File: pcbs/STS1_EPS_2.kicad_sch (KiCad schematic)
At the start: 12 parts, among them J1 Inter-EPS, J2 DS1, J3 DS2, J4 DS3, J5 DS4, J6 RBF, J7 Antenna Deployment, J8 UCI

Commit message: Worked on STS1_EPS_1 and STS1_EPS_2.
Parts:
- removed J1: Inter-EPS, Connector_PinHeader_2.00mm:PinHeader_2x07_P2.00mm_Vertical, symbol Connector_Generic:Conn_02x07_Odd_Even
- removed TP4: TestPoint, TestPoint:TestPoint_THTPad_D1.0mm_Drill0.5mm, symbol Connector:TestPoint
- added J1: Inter-EPS, Connector_PinHeader_2.00mm:PinHeader_2x10_P2.00mm_Vertical, symbol Connector_Generic:Conn_02x10_Odd_Even
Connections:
- net +5V: now also J1.2 (Pin_2)
- net BATT_RAW: now also J1.18 (Pin_18)
- net DS1_SIGNAL_1: now also J1.11 (Pin_11)
- net DS2_SIGNAL_1: now also J1.12 (Pin_12)
- net GND: now also J1.10 (Pin_10), J1.4 (Pin_4), J1.6 (Pin_6), J1.9 (Pin_9)
- net VOUT_I: now also J1.8 (Pin_8)
- net INTERNAL_V renamed Capacitor Bank/INTERNAL_V
- net Capacitor Bank/INTERNAL_V: now also J1.1 (Pin_1), J1.3 (Pin_3), J1.5 (Pin_5), J1.7 (Pin_7)
- new net BATT: J1.13 (Pin_13), J1.14 (Pin_14), J1.15 (Pin_15), J1.16 (Pin_16)
- new net BATT_I: J1.20 (Pin_20)
- new net CENTER: J1.17 (Pin_17)
- new net NTC: J1.19 (Pin_19)
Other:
- sheet Battery ports: added 5V, BATT, BATT_I, BATT_RAW, BAT_FAULT, CENTER, DS4_SIGNAL_1, NTC; removed none

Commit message: Worked on STS1_EPS_2.
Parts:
- renumbered J2 to J1, J3 to J2, J4 to J3, J5 to J4, J6 to J5, J7 to J6, J1 to J7
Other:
- sheet Battery State Detection ports: added UVLO_SIGNAL; removed none
- sheet Bus Gate ports: added UVLO_SIGNAL; removed none
- moved on the sheet: J8

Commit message: Worked on STS1_EPS_2.
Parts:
- removed J3: DS3, STS_Connector:M808420245, symbol Connector_Generic:Conn_01x02
- removed J4: DS4, STS_Connector:M808420245, symbol Connector_Generic:Conn_01x02
- added R3: 820, Resistor_SMD:R_0805_2012Metric, symbol Device:R
- added U8: TPS259472ARPW, STS_Package_DFN_QFN:TPS259472ARPWR, symbol STS_Power_Management:TPS259472ARPW
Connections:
- net BATT_RAW: now also U8.6 (OUT); no longer J8.1 (Pin_1)
- net GND: now also R3.1, U8.3 (PG), U8.4 (PGTH), U8.8 (GND)
- new net: J8.1 (Pin_1), U8.1 (EN/UVLO), U8.5 (IN)
- new net: R3.2, U8.9 (ILM)
- no-connect marks 4 -> 7
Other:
- sheet Battery ports: added DS1_SIGNAL, DS2_SIGNAL, RBF_SIGNAL, UVLO_SIGNAL; removed 5V, DS4_SIGNAL_1
- sheet Bus Gate ports: added DS1_SIGNAL; removed DS3_SIGNAL
- sheet CSBI ports: added UCI_COBC_UART_[1..2]; removed UCI_COBC_UART[1..2]
- sheet Deployment Switches + RBF ports: added DS1_SIGNAL_3, RBF_SIGNAL_3; removed +5V, DS3+, DS3-, DS3_SIGNAL_1, DS3_SIGNAL_2, DS4+, DS4-, DS4_SIGNAL_1, DS4_SIGNAL_2
- sheet Deployment Timer ports: added none; removed +5V, DS3_SIGNAL, DS4_SIGNAL
- note added: "Ideal diode, that ensures that the battery can not be discharged via the UCI."
- note added: "Sets ~4 A current limit."
- moved on the sheet: J1, J2, J5, J8, TP2

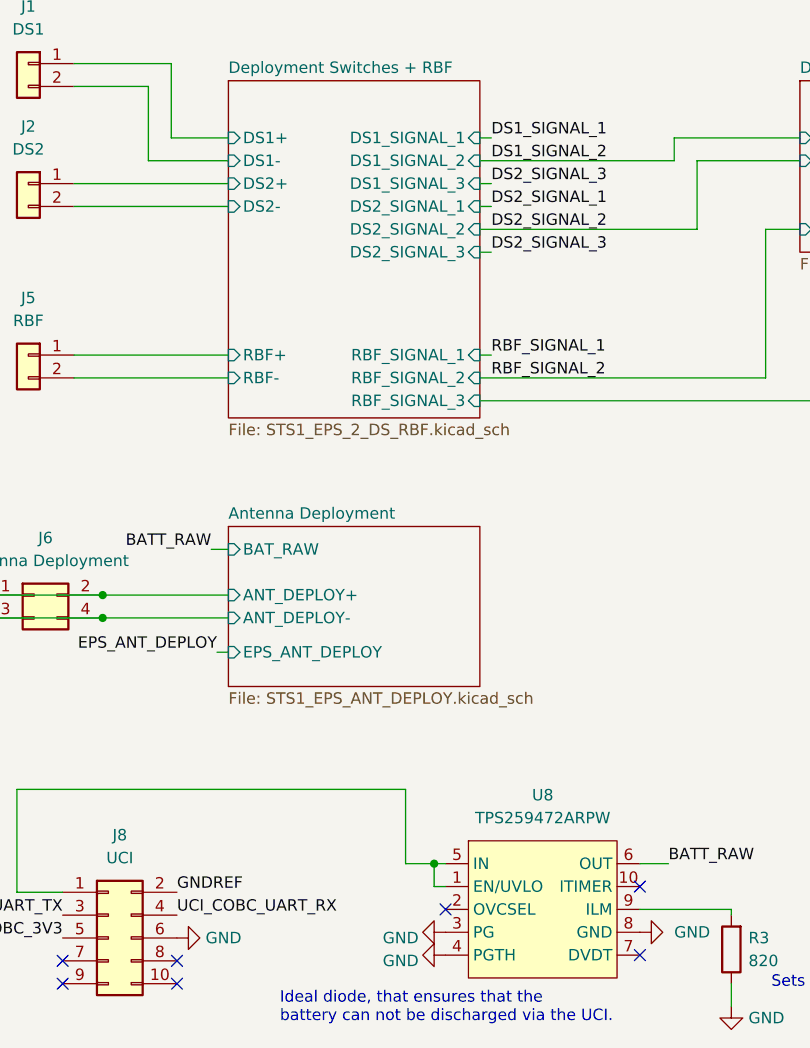
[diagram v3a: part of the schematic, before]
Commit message: STS1_EPS_2 no errors.
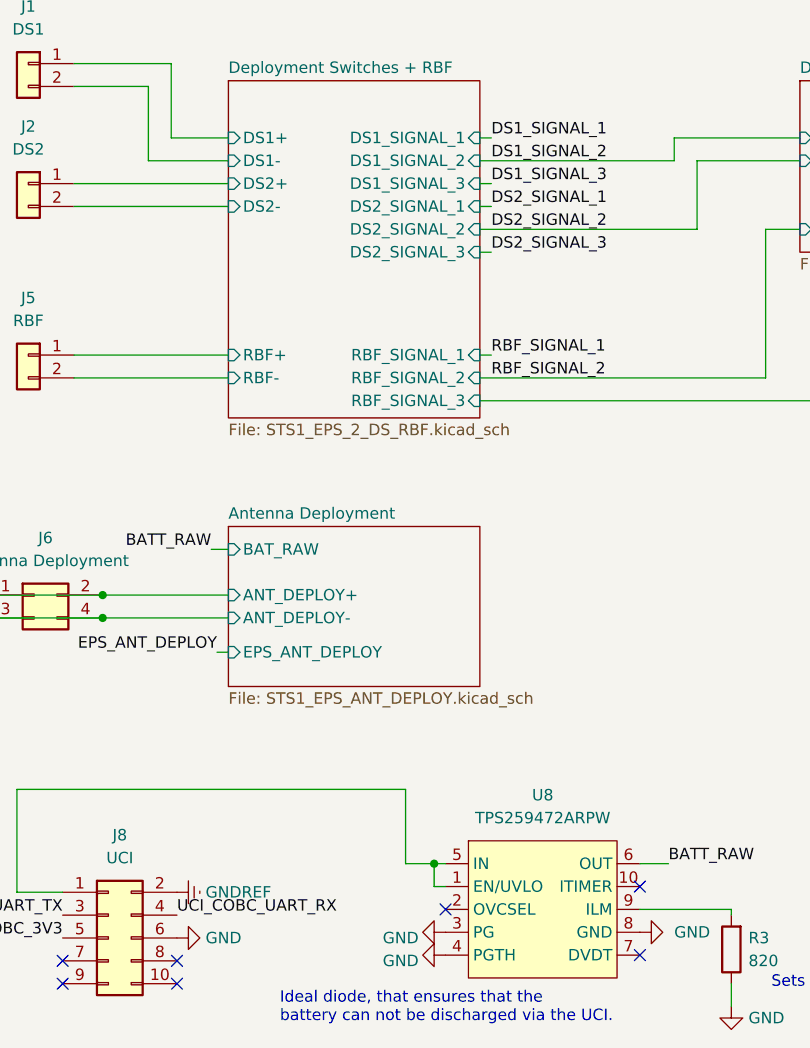
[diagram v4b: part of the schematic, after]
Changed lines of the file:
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@@
     (effects (font (size 1.27 1.27)) (justify left bottom))
   )
-  (label "DS2_SIGNAL_3" (at 78.74 101.6 0)
+  (label "DS1_SIGNAL_3" (at 78.74 101.6 0)
     (effects (font (size 1.27 1.27)) (justify left bottom))
   )
@@
   (label "DS1_SIGNAL_3" (at 190.5 149.225 180)
     (effects (font (size 1.27 1.27)) (justify right bottom))
-  )
-  (label "GNDREF" (at 43.815 180.34 0)
-    (effects (font (size 1.27 1.27)) (justify left bottom))
   )
   (label "BATT_RAW" (at 193.04 109.855 180)
@@
     )
     (property "Datasheet" "" (id 3) (at 40.64 48.26 0)
+      (effects (font (size 1.27 1.27)) hide)
+    )
+    (pin "1")
+  )
+  (symbol (lib_id "power:GNDREF") (at 43.815 180.34 90) (unit 1)
+    (in_bom yes) (on_board yes) (fields_autoplaced)
+    (property "Reference" "#PWR?" (id 0) (at 50.165 180.34 0)
+      (effects (font (size 1.27 1.27)) hide)
+    )
+    (property "Value" "GNDREF" (id 1) (at 46.99 180.3399 90)
+      (effects (font (size 1.27 1.27)) (justify right))
+    )
+    (property "Footprint" "" (id 2) (at 43.815 180.34 0)
+      (effects (font (size 1.27 1.27)) hide)
+    )
+    (property "Datasheet" "" (id 3) (at 43.815 180.34 0)
       (effects (font (size 1.27 1.27)) hide)
     )
@@
       (reference "#PWR0123") (unit 1) (value "~") (footprint "")
     )
+    (path "/782ccd28-d43b-446c-892c-2705ffe9f1f3/2f88d1c3-a8ed-418c-9a0c-3bcf014bd61e"
+      (reference "#PWR0124") (unit 1) (value "GND") (footprint "")
+    )
+    (path "/27387f3b-2bfa-4b28-8ff1-4907e84527b6"
+      (reference "#PWR?") (unit 1) (value "GNDREF") (footprint "")
+    )
     (path "/d08cc104-26df-403e-aeed-bb3c2e21e328/f818a80f-c894-4935-b466-2fb75a773837"
       (reference "C1") (unit 1) (value "100n") (footprint "Capacitor_SMD:C_0805_2012Metric")
@@
       (reference "C4") (unit 1) (value "100n") (footprint "Capacitor_SMD:C_0805_2012Metric")
     )
+    (path "/782ccd28-d43b-446c-892c-2705ffe9f1f3/bab6904b-9018-41a1-928c-c75a76fad2c6"
+      (reference "C5") (unit 1) (value "100n") (footprint "Capacitor_SMD:C_0805_2012Metric")
+    )
     (path "/f1424bad-2b95-4d34-bc23-e338e9fb6fbb/723f186f-e509-4f79-b697-dbc3026f5475"

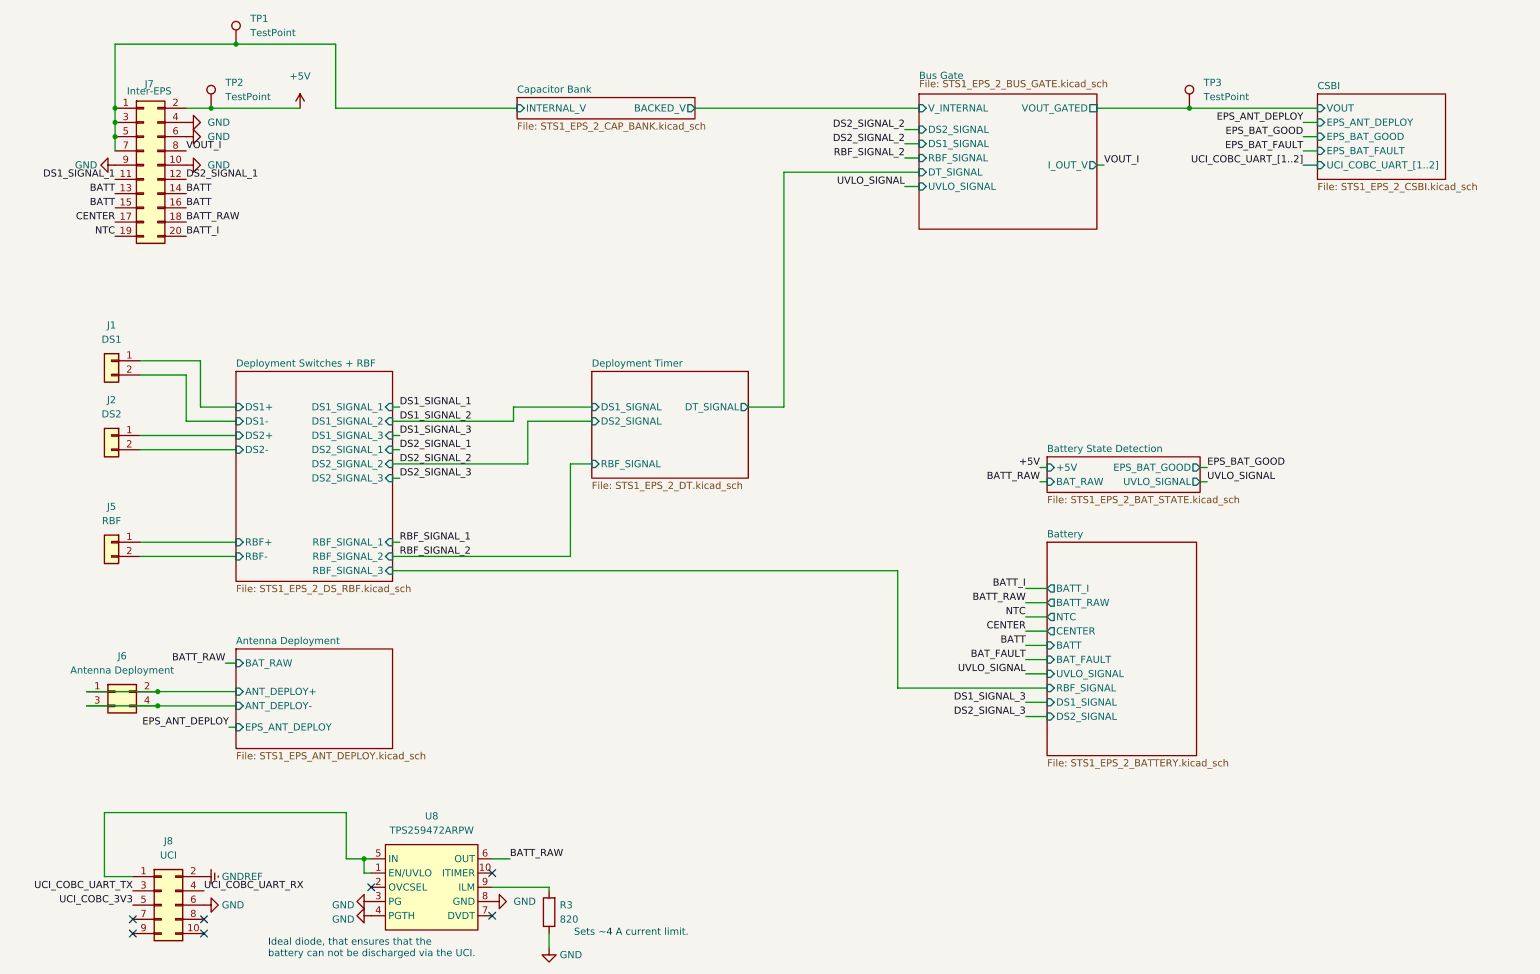
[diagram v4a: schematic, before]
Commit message: Added a logic voltage, so that the deployment circuit breaker FETs also work, when battery is fails.
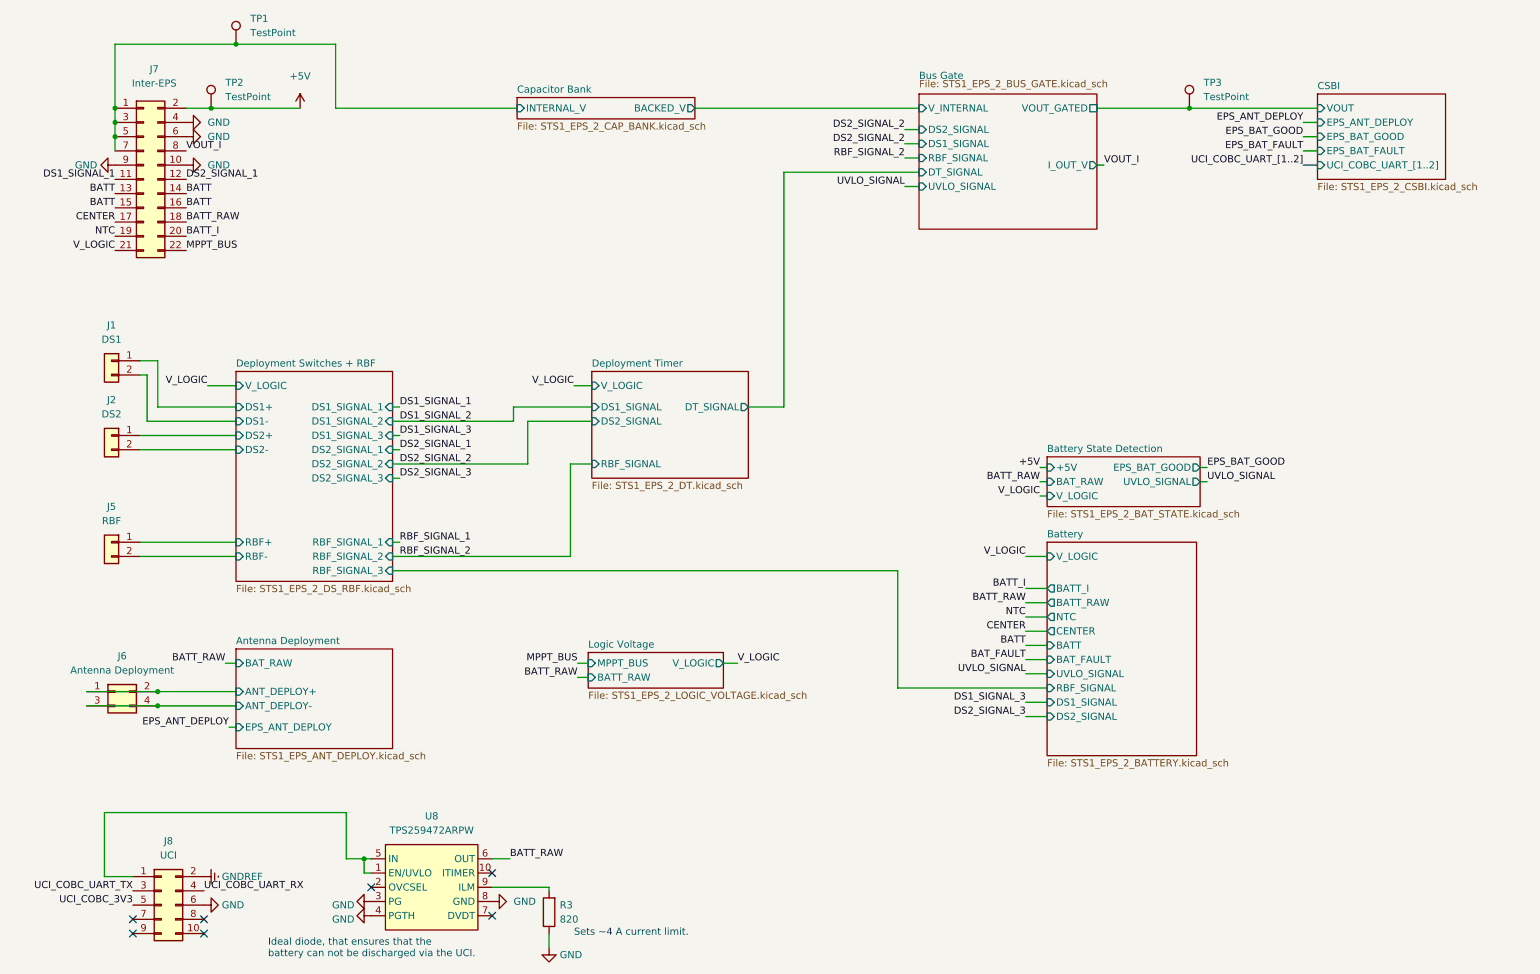
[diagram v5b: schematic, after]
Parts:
- J7: footprint Connector_PinHeader_2.00mm:PinHeader_2x10_P2.00mm_Vertical -> Connector_PinHeader_2.00mm:PinHeader_2x11_P2.00mm_Vertical; symbol Connector_Generic:Conn_02x10_Odd_Even -> Connector_Generic:Conn_02x11_Odd_Even
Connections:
- new net MPPT_BUS: J7.22 (Pin_22)
- new net V_LOGIC: J7.21 (Pin_21)
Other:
- added sheet Logic Voltage (STS1_EPS_2_LOGIC_VOLTAGE.kicad_sch)
- sheet Battery ports: added V_LOGIC; removed none
- sheet Battery State Detection ports: added V_LOGIC; removed none
- sheet Deployment Switches + RBF ports: added V_LOGIC; removed none
- sheet Deployment Timer ports: added V_LOGIC; removed none

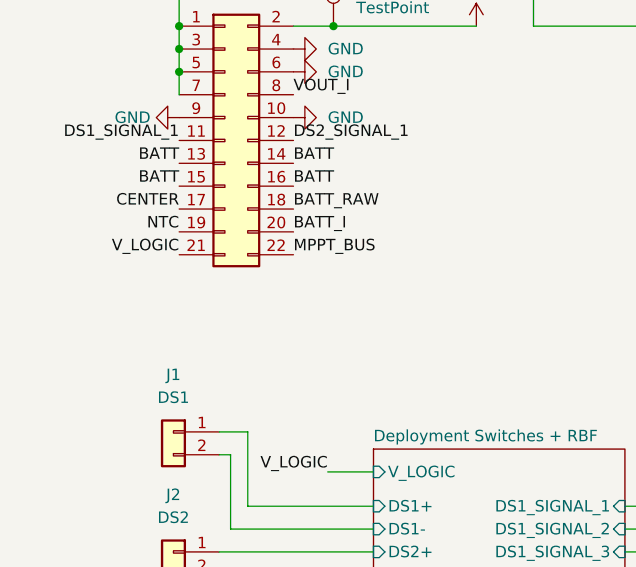
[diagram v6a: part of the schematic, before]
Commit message: Added part numbers to CSBI and inter EPS connectors. Also added some missing 3d files.
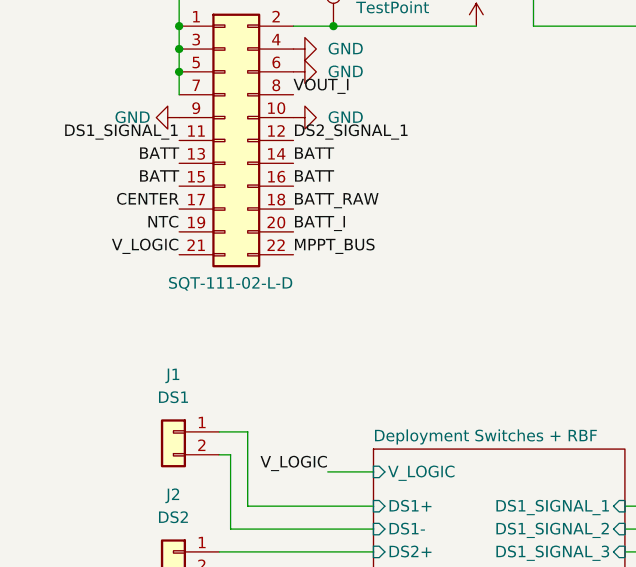
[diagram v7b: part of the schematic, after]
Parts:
- J7: Part# ESQT-107-02-F-D-800 -> SQT-111-02-L-D
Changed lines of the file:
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@@
       (effects (font (size 1.27 1.27)) hide)
     )
-    (property "Part#" "ESQT-107-02-F-D-800" (id 4) (at 33.02 55.88 0)
-      (effects (font (size 1.27 1.27)) hide)
-    )
+    (property "Part#" "SQT-111-02-L-D" (id 4) (at 33.655 71.755 0))
     (pin "1")
     (pin "10")
